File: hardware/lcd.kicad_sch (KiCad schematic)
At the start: 1 part, among them J2 Conn_01x40

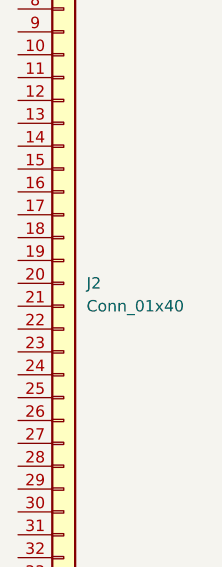
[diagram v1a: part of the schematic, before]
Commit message: update usb port, esd, lcsc
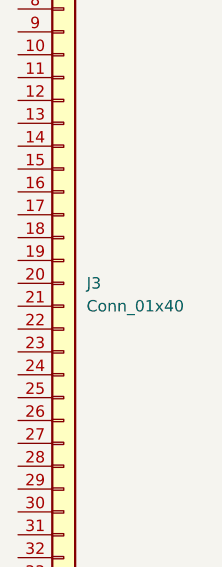
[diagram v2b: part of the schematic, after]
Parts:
- renumbered J2 to J3
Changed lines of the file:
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@@
 		(dnp no)
 		(fields_autoplaced yes)
-		(property "Reference" "J2"
+		(property "Reference" "J3"
 			(at 115.57 92.7099 0)
 			(effects
@@
 			(project "badge"
 				(path "/dc4a3d77-b0f8-4e90-a4be-3e93c7025348/ce5aa0f6-0554-44ba-9e09-c73e868ec9d0"
-					(reference "J2")
+					(reference "J3")
 					(unit 1)
 				)

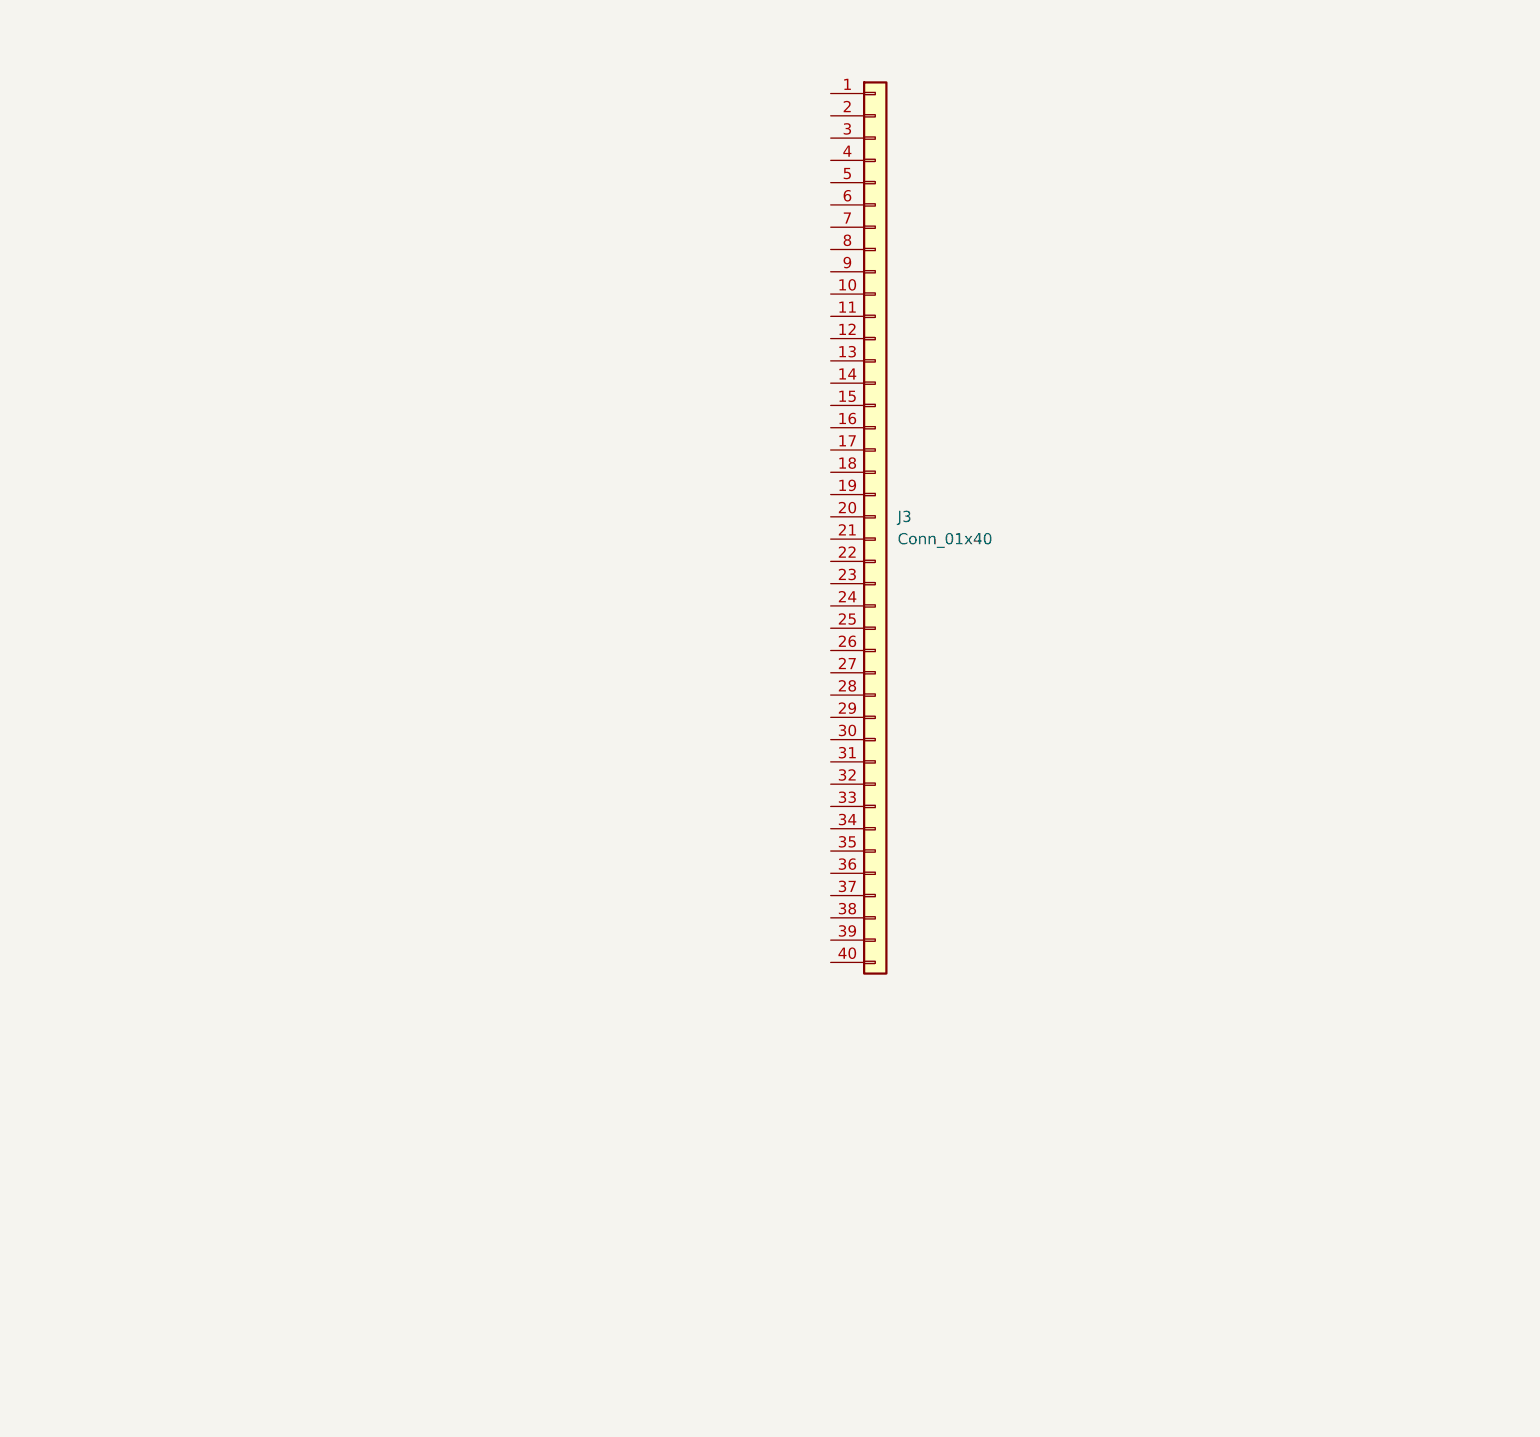
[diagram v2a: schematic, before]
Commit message: Initial schema of LCD interface
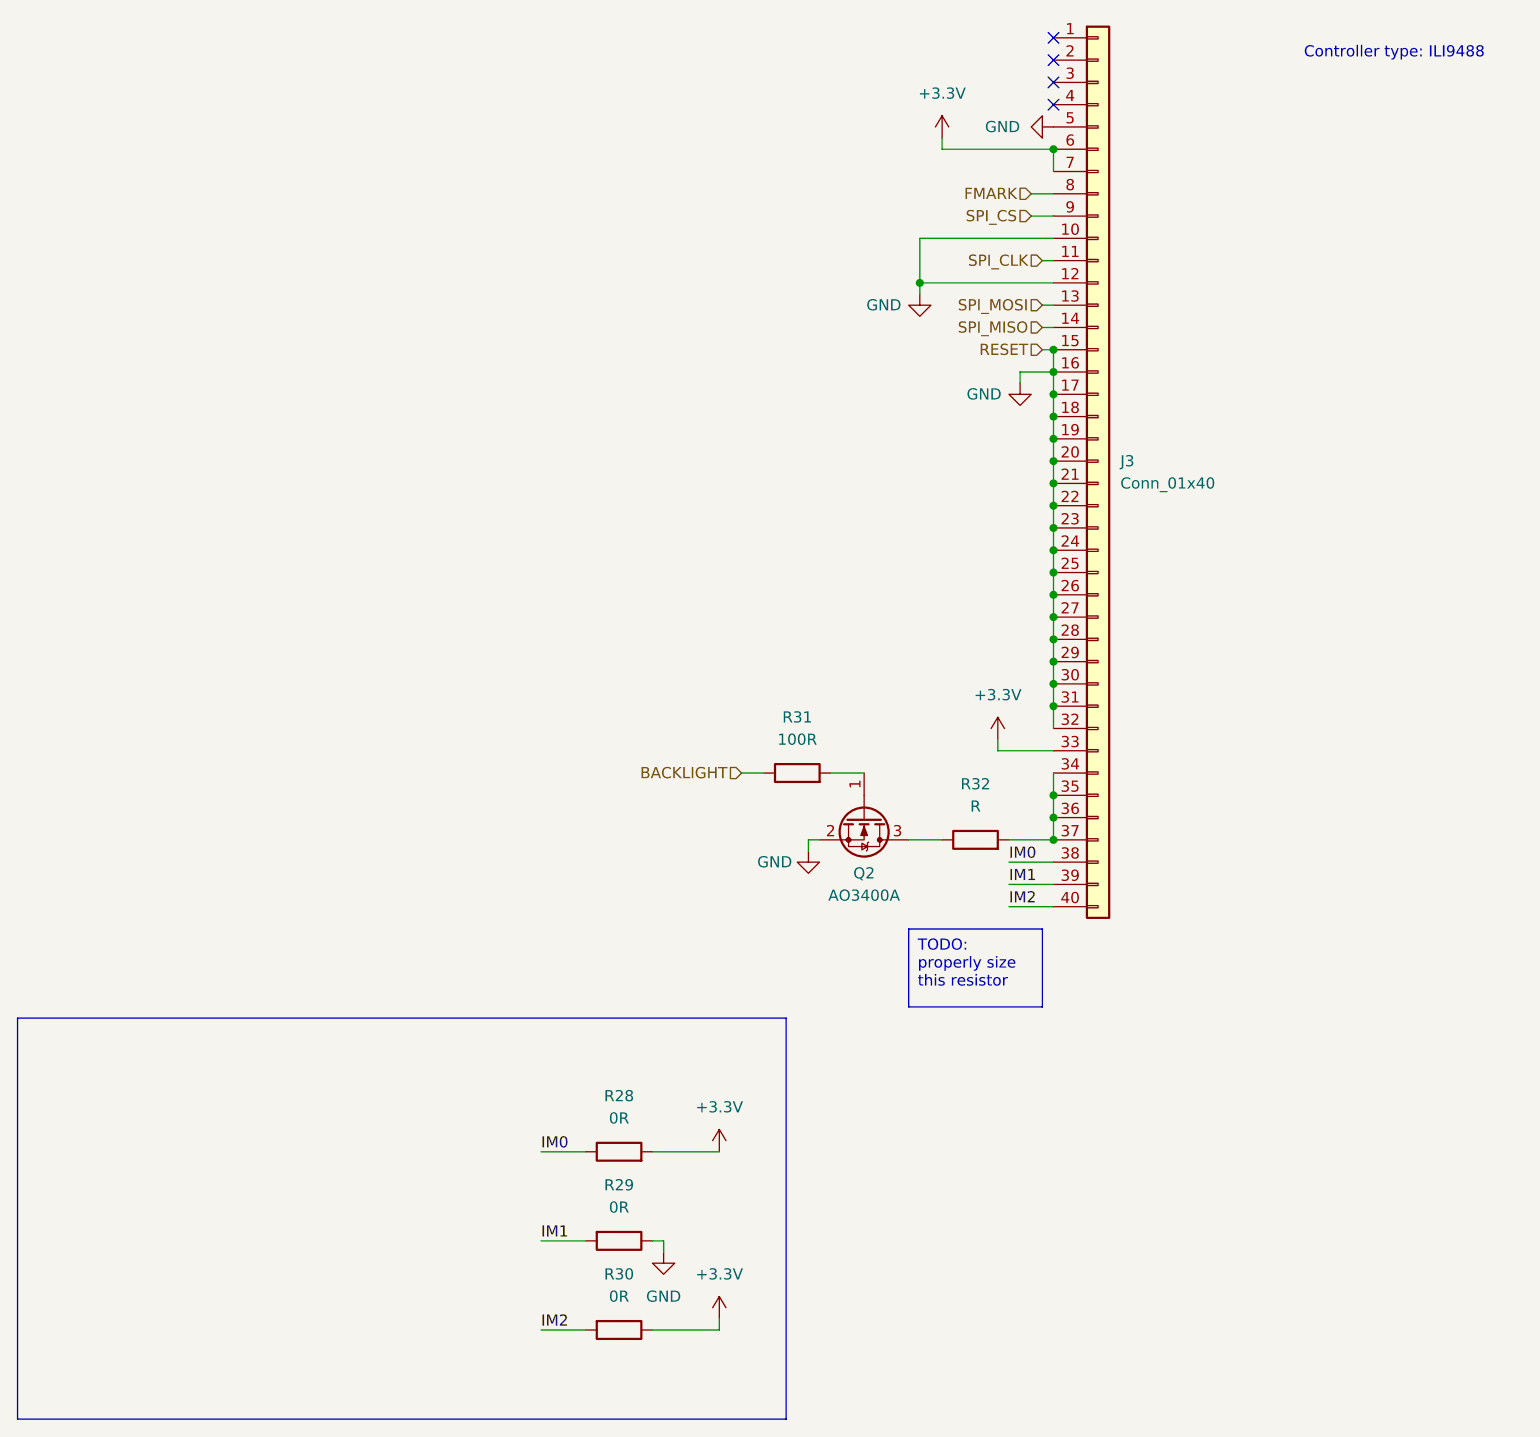
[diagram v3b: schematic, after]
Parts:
- added Q2: AO3400A, Package_TO_SOT_SMD:SOT-23, symbol Transistor_FET:AO3400A
- added R28, R29, R30: 0R, symbol Device:R
- added R31: 100R, symbol Device:R
- added R32: R, symbol Device:R
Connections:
- net GND: now reaches J3.10 (Pin_10)
- net GND: now also J3.12 (Pin_12), J3.15 (Pin_15), J3.16 (Pin_16), J3.17 (Pin_17), J3.18 (Pin_18), J3.19 (Pin_19), J3.20 (Pin_20), J3.21 (Pin_21), J3.22 (Pin_22), J3.23 (Pin_23), J3.24 (Pin_24), J3.25 (Pin_25), J3.26 (Pin_26), J3.27 (Pin_27), J3.28 (Pin_28), J3.29 (Pin_29), J3.30 (Pin_30), J3.31 (Pin_31), J3.32 (Pin_32), J3.5 (Pin_5), Q2.2 (S), R29.1
- net SPI_CLK: now reaches J3.11 (Pin_11)
- net SPI_MOSI: now reaches J3.13 (Pin_13)
- net SPI_MISO: now reaches J3.14 (Pin_14)
- net +3.3V: now reaches J3.33 (Pin_33)
- net +3.3V: now also J3.6 (Pin_6), J3.7 (Pin_7), R28.2, R30.1
- net at J3.34 (Pin_34): now also J3.35 (Pin_35), J3.36 (Pin_36), J3.37 (Pin_37), R32.2
- net IM0: now reaches J3.38 (Pin_38)
- net IM0: now also R28.1
- net IM1: now reaches J3.39 (Pin_39)
- net IM1: now also R29.2
- net IM2: now reaches J3.40 (Pin_40)
- net IM2: now also R30.2
- net FMARK: now reaches J3.8 (Pin_8)
- net SPI_CS: now reaches J3.9 (Pin_9)
- new net: Q2.3 (D), R32.1
- new net: Q2.1 (G), R31.2
- new net BACKLIGHT: R31.1
- no-connect marks 0 -> 4
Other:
- note added: "Controller type: ILI9488"
- moved on the sheet: J3

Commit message: lcd wires, wire direction
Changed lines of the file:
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@@
 	)
 	(hierarchical_label "SPI_MISO"
-		(shape input)
+		(shape output)
 		(at 132.08 71.12 180)
 		(fields_autoplaced yes)
@@
 	)
 	(hierarchical_label "FMARK"
-		(shape input)
+		(shape output)
 		(at 130.81 55.88 180)
 		(fields_autoplaced yes)

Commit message: Calculate approximate value of LED resistor
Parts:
- R32: value R -> 82R
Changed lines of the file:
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@@
 		)
 	)
-	(text_box "TODO: properly size this resistor"
+	(text_box "R32 needs to sink at least 1,64 mW"
 		(exclude_from_sim no)
 		(at 116.84 139.7 0)
@@
 			)
 		)
-		(property "Value" "R"
+		(property "Value" "82R"
 			(at 124.46 125.73 90)
 			(effects
